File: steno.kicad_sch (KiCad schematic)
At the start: 17 parts, among them J1 USB_C_Receptacle_USB2.0_14P, SW1 SW_Push, U2 AP2127N-3.3, U3 W25Q16JVSS

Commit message: Savepoint!
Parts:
- C10, C11, C12, C13, C4, C5, C9: footprint (none) -> Capacitor_Tantalum_SMD:CP_EIA-1608-08_AVX-J_HandSolder
- D1: footprint (none) -> Diode_SMD:D_SOD-123
- J1: footprint (none) -> Connector_USB:USB_C_Receptacle_HRO_TYPE-C-31-M-12
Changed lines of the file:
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@@
 			)
 		)
-		(property "Footprint" ""
+		(property "Footprint" "Capacitor_Tantalum_SMD:CP_EIA-1608-08_AVX-J_HandSolder"
 			(at 110.1852 29.21 0)
 			(hide yes)
@@
 			)
 		)
-		(property "Footprint" ""
+		(property "Footprint" "Capacitor_Tantalum_SMD:CP_EIA-1608-08_AVX-J_HandSolder"
 			(at 72.0852 29.21 0)
 			(hide yes)
@@
 			)
 		)
-		(property "Footprint" ""
+		(property "Footprint" "Capacitor_Tantalum_SMD:CP_EIA-1608-08_AVX-J_HandSolder"
 			(at 101.2952 29.21 0)
 			(hide yes)
@@
 			)
 		)
-		(property "Footprint" ""
+		(property "Footprint" "Capacitor_Tantalum_SMD:CP_EIA-1608-08_AVX-J_HandSolder"
 			(at 80.9752 29.21 0)
 			(hide yes)
@@
 			)
 		)
-		(property "Footprint" ""
+		(property "Footprint" "Connector_USB:USB_C_Receptacle_HRO_TYPE-C-31-M-12"
 			(at 33.02 36.83 0)
 			(hide yes)
@@
 			)
 		)
-		(property "Footprint" ""
+		(property "Footprint" "Diode_SMD:D_SOD-123"
 			(at 60.96 21.59 0)
 			(hide yes)
@@
 			)
 		)
-		(property "Footprint" ""
+		(property "Footprint" "Capacitor_Tantalum_SMD:CP_EIA-1608-08_AVX-J_HandSolder"
 			(at 73.3552 101.6 0)
 			(hide yes)
@@
 			)
 		)
-		(property "Footprint" ""
+		(property "Footprint" "Capacitor_Tantalum_SMD:CP_EIA-1608-08_AVX-J_HandSolder"
 			(at 22.5552 67.31 0)
 			(hide yes)
@@
 			)
 		)
-		(property "Footprint" ""
+		(property "Footprint" "Capacitor_Tantalum_SMD:CP_EIA-1608-08_AVX-J_HandSolder"
 			(at 89.8652 101.6 0)
 			(hide yes)

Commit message: Savepoint!
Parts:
- D1: footprint Diode_SMD:D_SOD-123 -> Diode_SMD:D_SOD-323F
- SW1: footprint (none) -> Button_Switch_THT:SW_PUSH_6mm
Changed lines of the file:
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@@
 			)
 		)
-		(property "Footprint" "Diode_SMD:D_SOD-123"
+		(property "Footprint" "Diode_SMD:D_SOD-323F"
 			(at 60.96 21.59 0)
 			(hide yes)
@@
 			)
 		)
-		(property "Footprint" ""
+		(property "Footprint" "Button_Switch_THT:SW_PUSH_6mm"
 			(at 36.83 87.63 0)
 			(hide yes)

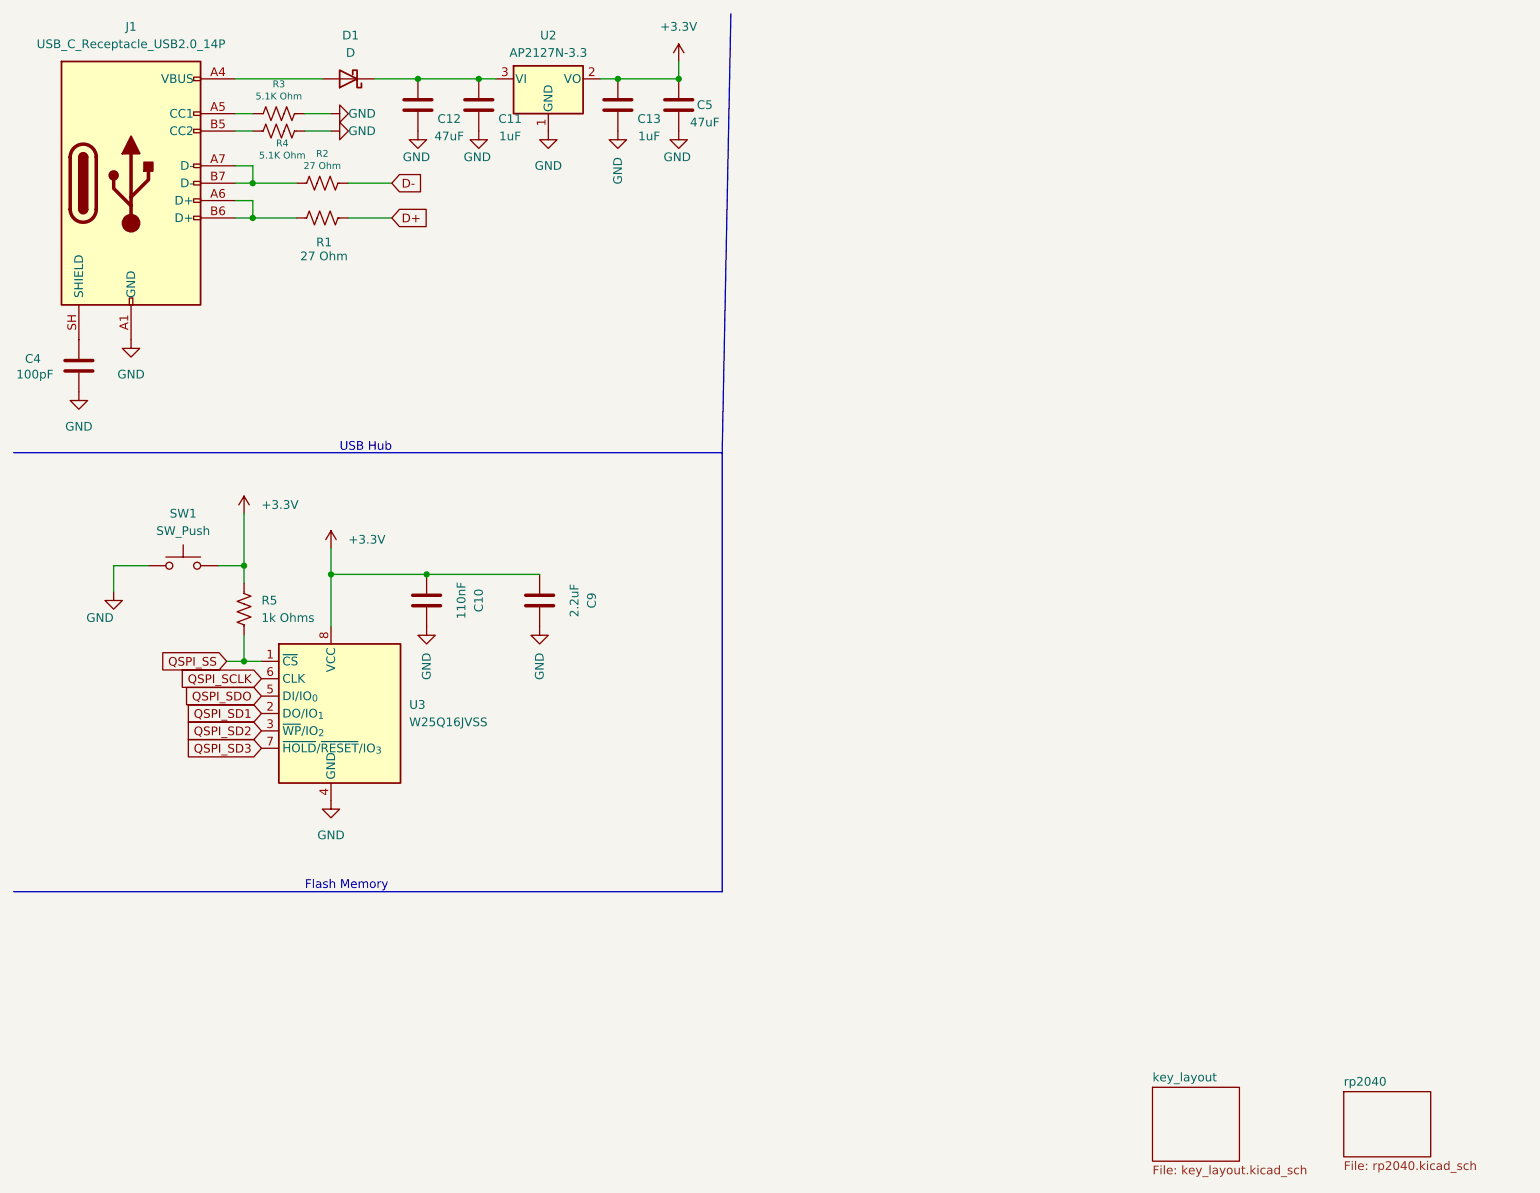
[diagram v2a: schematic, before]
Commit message: Smalled Caps and Restarting Layout.
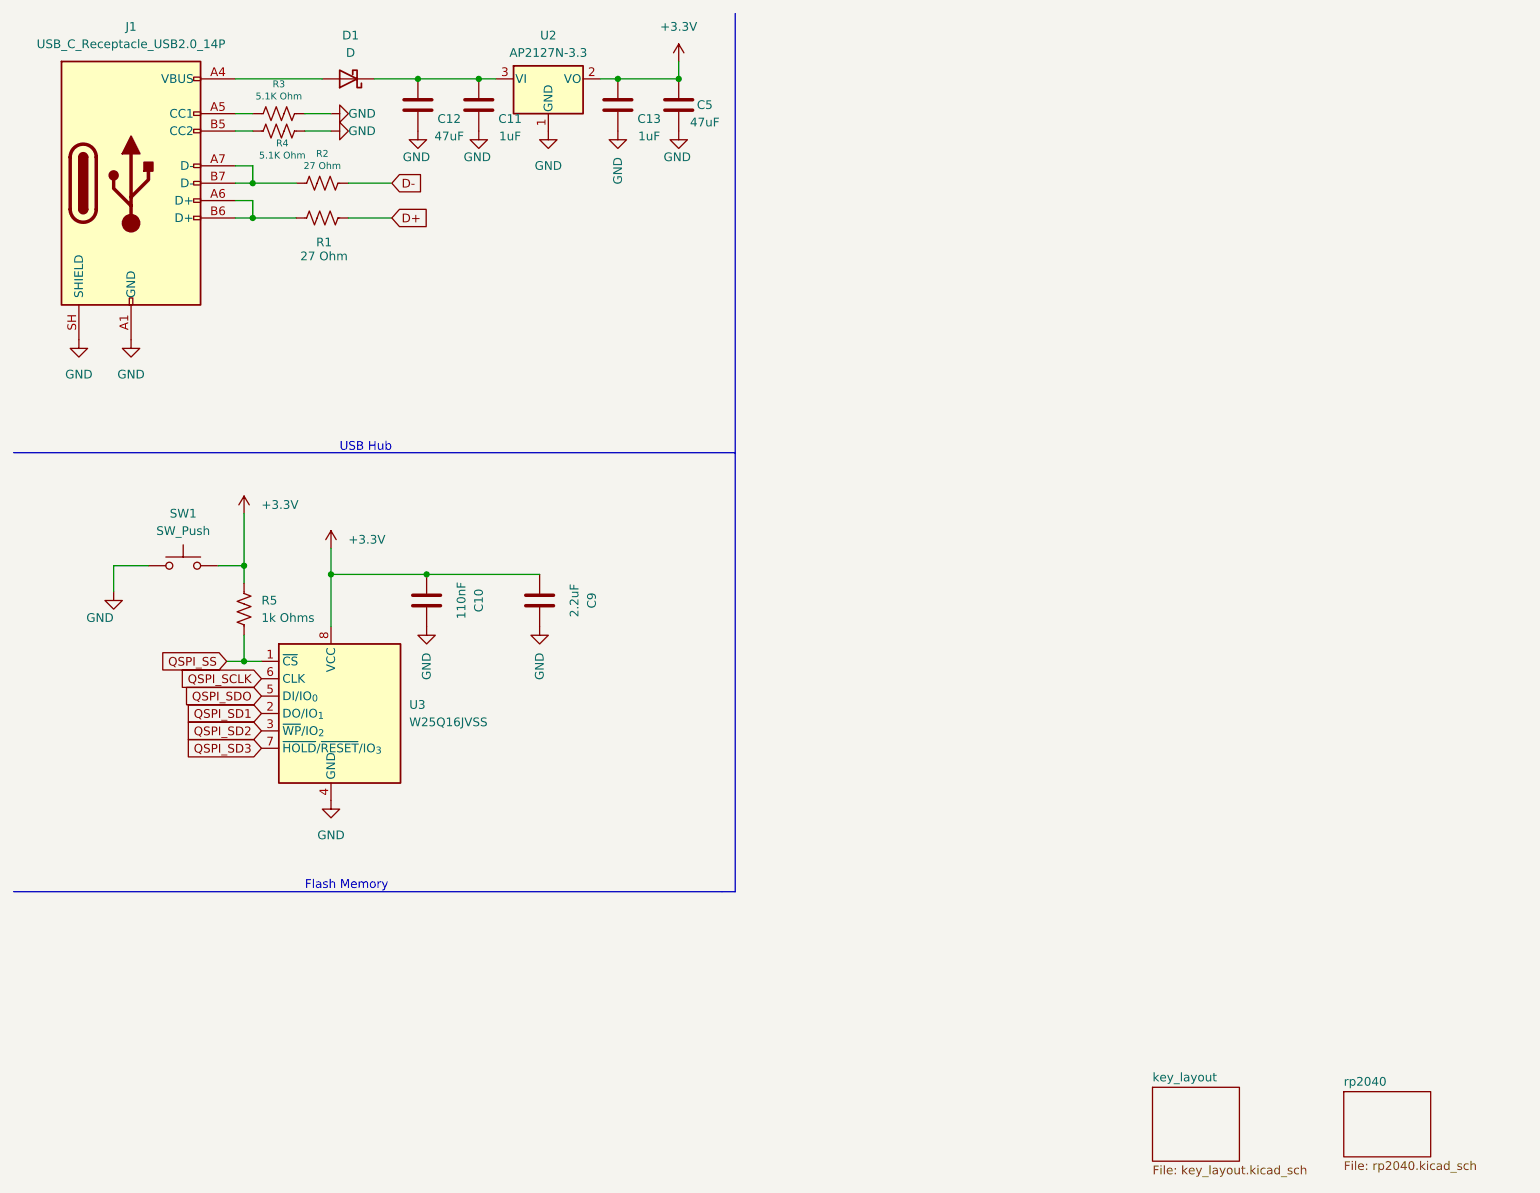
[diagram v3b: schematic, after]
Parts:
- removed C4: 100pF, Capacitor_Tantalum_SMD:CP_EIA-1608-08_AVX-J_HandSolder, symbol Device:C
- C10, C11, C12, C13, C5, C9: footprint Capacitor_Tantalum_SMD:CP_EIA-1608-08_AVX-J_HandSolder -> Capacitor_SMD:C_0402_1005Metric_Pad0.74x0.62mm_HandSolder
- R1, R2, R3, R4, R5: footprint (none) -> Resistor_SMD:R_0402_1005Metric_Pad0.72x0.64mm_HandSolder
- SW1: footprint Button_Switch_THT:SW_PUSH_6mm -> ScottoKeebs_Components:Button_MJTP1243
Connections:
- net GND: now also J1.SH (SHIELD)
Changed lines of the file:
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@@
 	(polyline
 		(pts
-			(xy 116.84 12.065) (xy 115.57 76.2)
+			(xy 117.475 12.065) (xy 117.475 76.2)
 		)
 		(stroke
@@
 	(polyline
 		(pts
-			(xy 12.065 76.2) (xy 115.57 76.2)
+			(xy 12.065 76.2) (xy 117.475 76.2)
 		)
 		(stroke
@@
 		)
 	)
+	(polyline
+		(pts
+			(xy 115.57 140.335) (xy 117.475 140.335)
+		)
+		(stroke
+			(width 0)
+			(type default)
+		)
+	)
 	(wire
 		(pts
@@
 	(polyline
 		(pts
-			(xy 115.57 140.335) (xy 115.57 76.2)
+			(xy 117.475 140.335) (xy 117.475 76.2)
 		)
 		(stroke
@@
 			)
 		)
-		(property "Footprint" "Capacitor_Tantalum_SMD:CP_EIA-1608-08_AVX-J_HandSolder"
+		(property "Footprint" "Capacitor_SMD:C_0402_1005Metric_Pad0.74x0.62mm_HandSolder"
 			(at 110.1852 29.21 0)
 			(hide yes)
@@
 			)
 		)
-		(property "Footprint" ""
+		(property "Footprint" "Resistor_SMD:R_0402_1005Metric_Pad0.72x0.64mm_HandSolder"
 			(at 51.054 25.654 90)
 			(hide yes)
@@
 			)
 		)
-		(property "Footprint" "Capacitor_Tantalum_SMD:CP_EIA-1608-08_AVX-J_HandSolder"
+		(property "Footprint" "Capacitor_SMD:C_0402_1005Metric_Pad0.74x0.62mm_HandSolder"
 			(at 72.0852 29.21 0)
 			(hide yes)
@@
 			)
 		)
-		(property "Footprint" "Capacitor_Tantalum_SMD:CP_EIA-1608-08_AVX-J_HandSolder"
+		(property "Footprint" "Capacitor_SMD:C_0402_1005Metric_Pad0.74x0.62mm_HandSolder"
 			(at 101.2952 29.21 0)
 			(hide yes)
@@
 			)
 		)
-		(property "Footprint" "Capacitor_Tantalum_SMD:CP_EIA-1608-08_AVX-J_HandSolder"
+		(property "Footprint" "Capacitor_SMD:C_0402_1005Metric_Pad0.74x0.62mm_HandSolder"
 			(at 80.9752 29.21 0)
 			(hide yes)
@@
 			)
 		)
-		(property "Footprint" ""
+		(property "Footprint" "Resistor_SMD:R_0402_1005Metric_Pad0.72x0.64mm_HandSolder"
 			(at 57.404 40.894 90)
 			(hide yes)
@@
 			)
 		)
-		(property "Footprint" ""
+		(property "Footprint" "Resistor_SMD:R_0402_1005Metric_Pad0.72x0.64mm_HandSolder"
 			(at 51.054 28.194 90)
 			(hide yes)
@@
 	(symbol
 		(lib_id "power:GND")
-		(at 21.59 67.31 0)
+		(at 21.59 59.69 0)
 		(unit 1)
 		(body_style 1)
@@
 		(fields_autoplaced yes)
 		(property "Reference" "#PWR011"
-			(at 21.59 73.66 0)
+			(at 21.59 66.04 0)
 			(hide yes)
 			(show_name no)
@@
 		)
 		(property "Value" "GND"
-			(at 21.59 72.39 0)
+			(at 21.59 64.77 0)
 			(show_name no)
 			(do_not_autoplace no)
@@
 		)
 		(property "Footprint" ""
-			(at 21.59 67.31 0)
+			(at 21.59 59.69 0)
 			(hide yes)
 			(show_name no)
@@
 		)
 		(property "Datasheet" ""
-			(at 21.59 67.31 0)
+			(at 21.59 59.69 0)
 			(hide yes)
 			(show_name no)
@@
 		)
 		(property "Description" "Power symbol creates a global label with name \"GND\" , ground"
-			(at 21.59 67.31 0)
+			(at 21.59 59.69 0)
 			(hide yes)
 			(show_name no)
@@
 			)
 		)
-		(property "Footprint" ""
+		(property "Footprint" "Resistor_SMD:R_0402_1005Metric_Pad0.72x0.64mm_HandSolder"
 			(at 46.736 99.314 90)
 			(hide yes)
@@
 			)
 		)
-		(property "Footprint" ""
+		(property "Footprint" "Resistor_SMD:R_0402_1005Metric_Pad0.72x0.64mm_HandSolder"
 			(at 57.404 35.814 90)
 			(hide yes)
@@
 			)
 		)
-		(property "Footprint" "Capacitor_Tantalum_SMD:CP_EIA-1608-08_AVX-J_HandSolder"
+		(property "Footprint" "Capacitor_SMD:C_0402_1005Metric_Pad0.74x0.62mm_HandSolder"
 			(at 73.3552 101.6 0)
 			(hide yes)
@@
 			)
 		)
-		(property "Footprint" "Button_Switch_THT:SW_PUSH_6mm"
+		(property "Footprint" "ScottoKeebs_Components:Button_MJTP1243"
 			(at 36.83 87.63 0)
 			(hide yes)
@@
 	)
 	(symbol
-		(lib_id "Device:C")
-		(at 21.59 63.5 0)
-		(unit 1)
-		(body_style 1)
-		(exclude_from_sim no)
-		(in_bom yes)
-		(on_board yes)
-		(in_pos_files yes)
-		(dnp no)
-		(property "Reference" "C4"
-			(at 13.716 62.484 0)
-			(show_name no)
-			(do_not_autoplace no)
-			(effects
-				(font
-					(size 1.27 1.27)
-				)
-				(justify left)
-			)
-		)
-		(property "Value" "100pF"
-			(at 12.446 64.77 0)
-			(show_name no)
-			(do_not_autoplace no)
-			(effects
-				(font
-					(size 1.27 1.27)
-				)
-				(justify left)
-			)
-		)
-		(property "Footprint" "Capacitor_Tantalum_SMD:CP_EIA-1608-08_AVX-J_HandSolder"
-			(at 22.5552 67.31 0)
-			(hide yes)
-			(show_name no)
-			(do_not_autoplace no)
-			(effects
-				(font
-					(size 1.27 1.27)
-				)
-			)
-		)
-		(property "Datasheet" ""
-			(at 21.59 63.5 0)
-			(hide yes)
-			(show_name no)
-			(do_not_autoplace no)
-			(effects
-				(font
-					(size 1.27 1.27)
-				)
-			)
-		)
-		(property "Description" "Unpolarized capacitor"
-			(at 21.59 63.5 0)
-			(hide yes)
-			(show_name no)
-			(do_not_autoplace no)
-			(effects
-				(font
-					(size 1.27 1.27)
-				)
-			)
-		)
-		(pin "1"
-		)
-		(pin "2"
-		)
-		(instances
-			(project "steno"
-				(path "/238e1d3b-9ec5-448b-85c7-386a29cd2631"
-					(reference "C4")
-					(unit 1)
-				)
-			)
-		)
-	)
-	(symbol
 		(lib_id "power:+3.3V")
 		(at 58.42 90.17 0)
@@
 			)
 		)
-		(property "Footprint" "Capacitor_Tantalum_SMD:CP_EIA-1608-08_AVX-J_HandSolder"
+		(property "Footprint" "Capacitor_SMD:C_0402_1005Metric_Pad0.74x0.62mm_HandSolder"
 			(at 89.8652 101.6 0)
 			(hide yes)

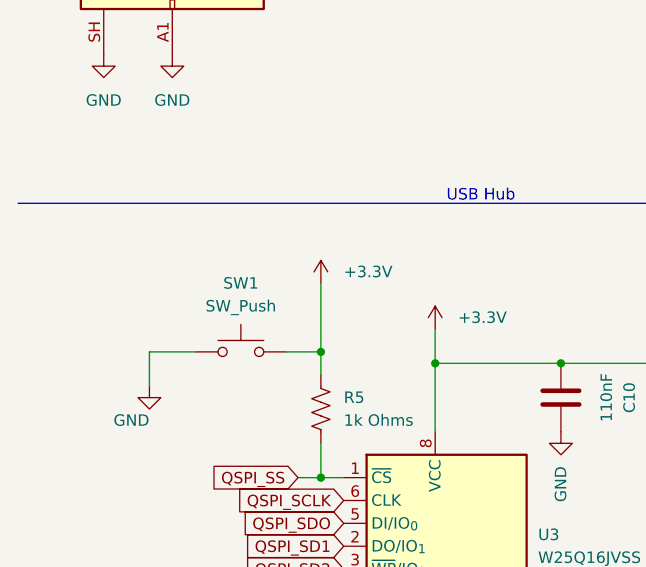
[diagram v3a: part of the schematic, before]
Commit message: Layout changes & wiring testing
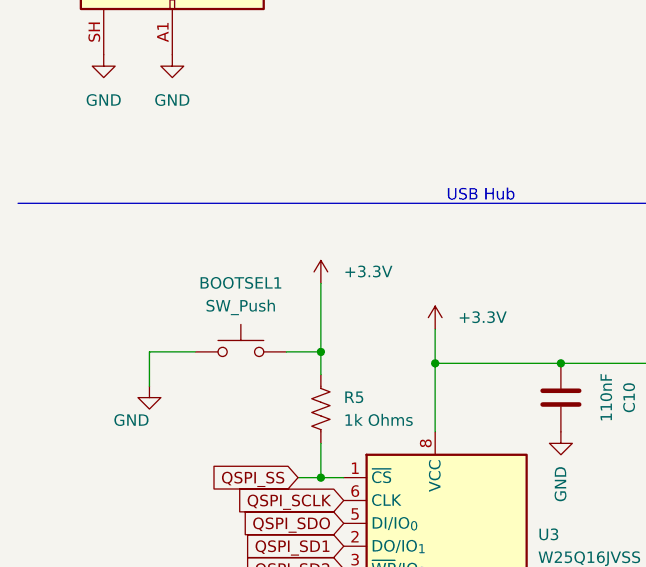
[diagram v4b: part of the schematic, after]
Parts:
- renumbered SW1 to BOOTSEL1
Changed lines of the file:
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@@
 		(dnp no)
 		(fields_autoplaced yes)
-		(property "Reference" "SW1"
+		(property "Reference" "BOOTSEL1"
 			(at 36.83 85.09 0)
 			(show_name no)
@@
 			(project "steno"
 				(path "/238e1d3b-9ec5-448b-85c7-386a29cd2631"
-					(reference "SW1")
+					(reference "BOOTSEL1")
 					(unit 1)
 				)
